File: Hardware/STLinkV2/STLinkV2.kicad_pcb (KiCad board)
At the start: 2 copper layers, 73.7 x 38.1 mm, 62 parts, among them J1 USB_B_Micro, J2 SWD, J3 ISP, J4 RS232, J5 JTAG, U1 STM32F103CBT6, U2 SRV05-4, U3 HT7833, U4 SRV05-4, U5 SRV05-4, U6 74AVCH2T45DC,125, U7 74AVCH2T45DC,125, Y1 8MHz

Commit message: Final review of 'STLinkV2' and fabrication output.
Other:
- rule pad_to_mask_clearance: 0.1 -> 0
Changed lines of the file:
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@@
       (dielectric_constraints no)
     )
-    (pad_to_mask_clearance 0.1)
-    (solder_mask_min_width 0.2)
+    (pad_to_mask_clearance 0)
     (grid_origin 63.5 50.8)
     (pcbplotparams

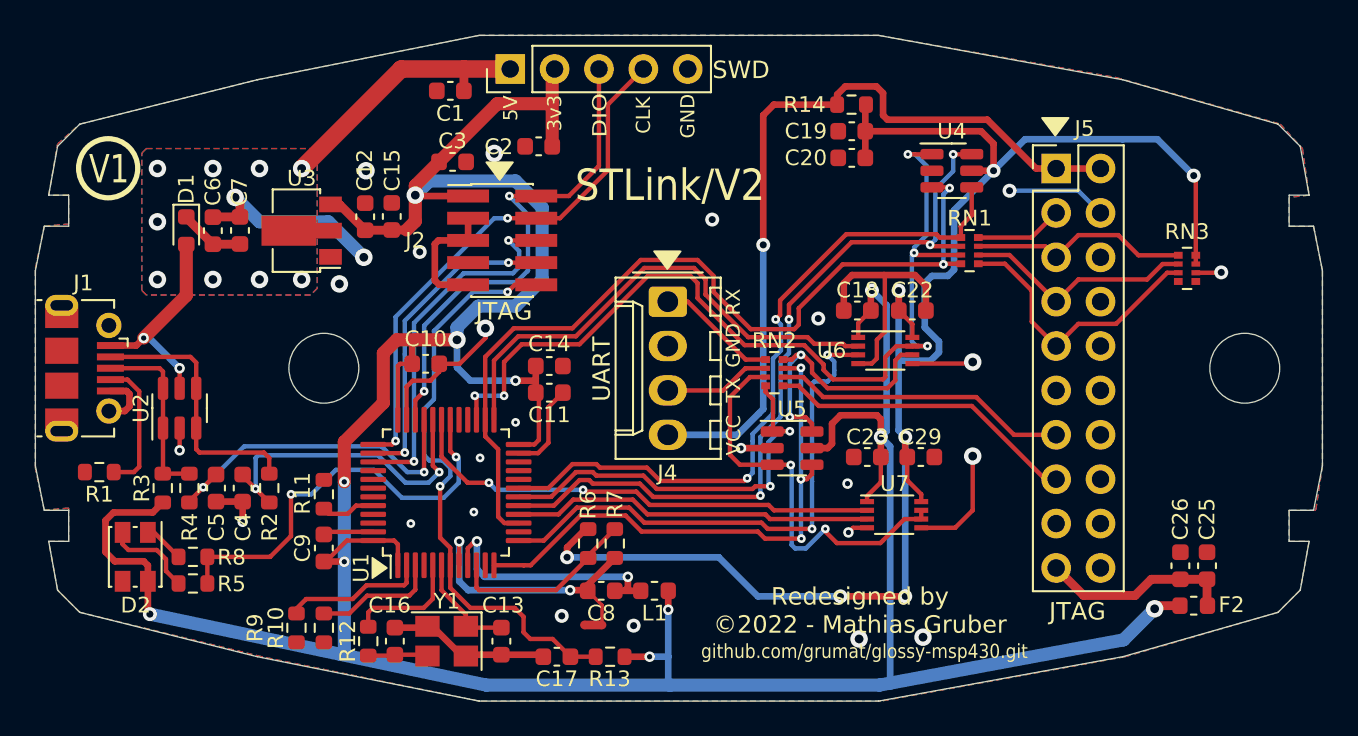
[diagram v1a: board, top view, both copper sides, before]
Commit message: Minor fixes on the STLinkV2 board (no new version is required)
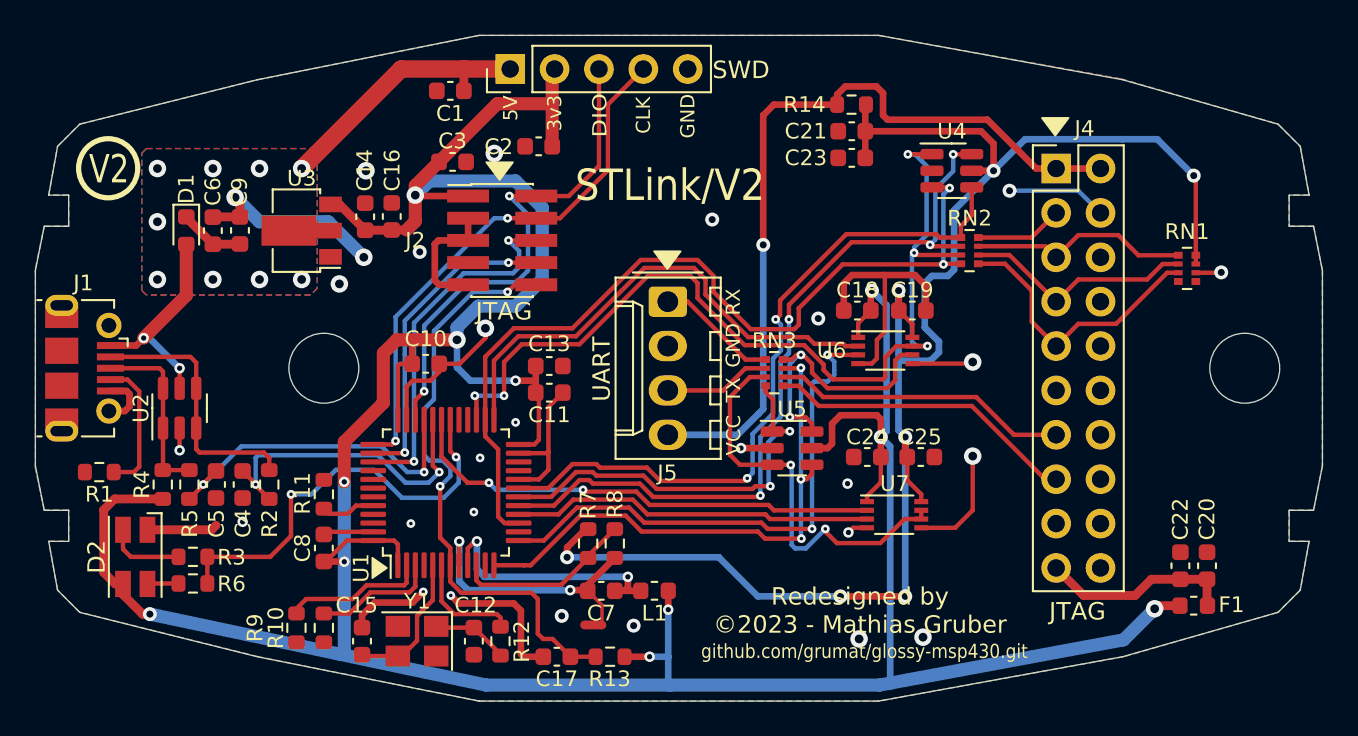
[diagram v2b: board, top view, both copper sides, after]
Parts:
- C12: renamed from C13; value 20pF -> 4.7pF
- C15: renamed from C16; value 20pF -> 4.7pF
- D2: footprint LED_SMD:LED_Kingbright_AAA3528ESGCT -> LED_SMD:LED_RGB_Wuerth-PLCC4_3.2x2.8mm_150141M173100
- R12: value 2k -> 470
- moved R12 7.57 mm to (90.1, 85.5)
- moved C15 1.88 mm to (82.2, 85.5)
- moved Y1 1.69 mm to (85.3, 85.5)
- moved C12 1.57 mm to (88.6, 85.5)
- moved R3 1.52 mm to (72.5, 80.6)
- moved R6 1.52 mm to (72.5, 82.2)
- moved C4 0.20 mm to (75.4, 76.5)
- moved C5 0.20 mm to (73.8, 76.5)
- moved R2 0.20 mm to (76.9, 76.5)
- moved R4 0.20 mm to (70.8, 76.5)
- moved R5 0.20 mm to (72.3, 76.5)
- renumbered C14 to C13, C12 to C14, C15 to C16, C22 to C19, C25 to C20, C19 to C21, C26 to C22, C20 to C23, C23 to C24, C29 to C25, C8 to C7, C9 to C8, C7 to C9, F2 to F1, J5 to J4, J4 to J5, R5 to R3, R3 to R4, R4 to R5, R8 to R6, R6 to R7, R7 to R8, RN3 to RN1, RN1 to RN2, RN2 to RN3
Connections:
- C12 pad 1: /OSC_OUT -> Net-(C12-Pad1)
- C15 pad 1: Net-(C16-Pad1) -> /OSC_IN
- R12 pad 1: Net-(C16-Pad1) -> Net-(C12-Pad1)
- R12 pad 2: /OSC_IN -> /OSC_OUT
- U1 pad 20: unconnected-(U1-Pad20) -> GND
- Y1 pad 1: /OSC_OUT -> Net-(C12-Pad1)
- Y1 pad 3: Net-(C16-Pad1) -> /OSC_IN
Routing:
- net GND: track 86.2 -> 94.5 mm, vias 26 -> 28
- net Net-(C12-Pad1): track 0.00 -> 4.41 mm
- net Net-(C16-Pad1): track 3.44 -> 0.00 mm
- net /OSC_IN: track 6.76 -> 8.24 mm
- net Net-(D2-Pad4): track 5.20 -> 4.47 mm
- net Net-(D2-Pad1): track 2.33 -> 1.79 mm
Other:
- board text added: "Redesigned by ©2023 - Mathias Gruber"
- board text added: "V2"
- board text removed: "Redesigned by ©2022 - Mathias Gruber"
- board text removed: "V1"

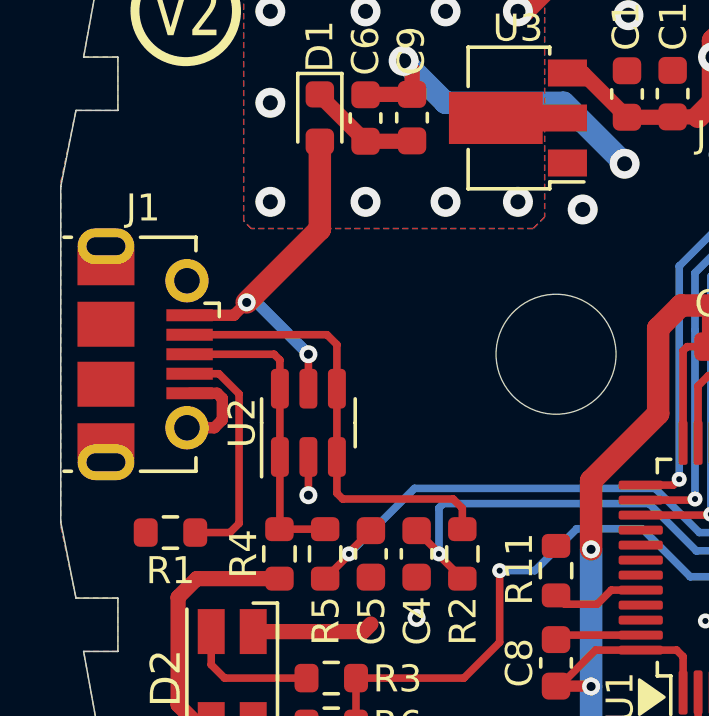
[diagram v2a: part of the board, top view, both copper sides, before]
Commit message: Fixes on USB ESD protection
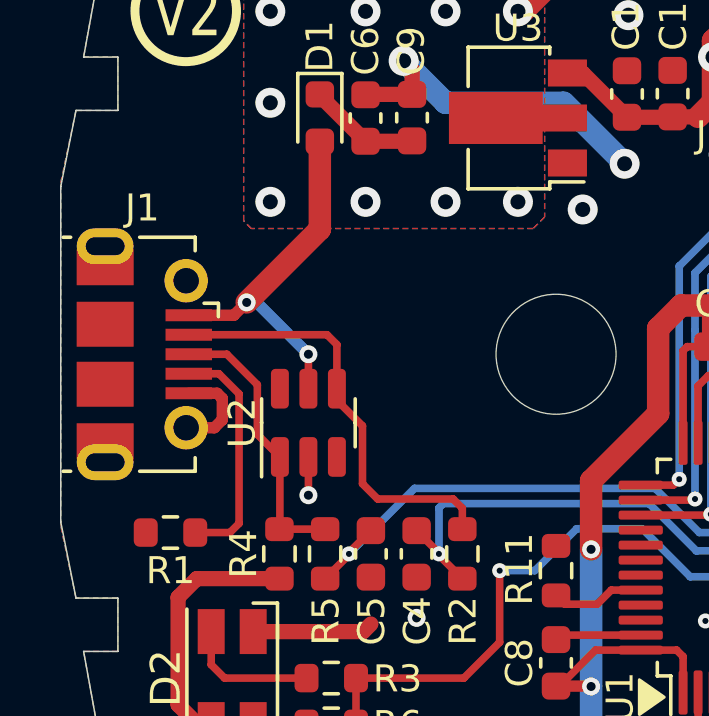
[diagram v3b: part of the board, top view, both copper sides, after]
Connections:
- U2 pad 3: /E_USB- -> unconnected-(U2-Pad3)
- U2 pad 6: /E_USB+ -> unconnected-(U2-Pad6)
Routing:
- net /E_USB+: track 10.3 -> 9.36 mm
- net /E_USB-: track 15.1 -> 14.4 mm
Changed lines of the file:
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@@
   (net 66 "unconnected-(RN1-Pad5)")
   (net 67 "Net-(R9-Pad2)")
+  (net 68 "unconnected-(U2-Pad3)")
+  (net 69 "unconnected-(U2-Pad6)")
   (footprint "Capacitor_SMD:C_0603_1608Metric" (layer "F.Cu")
     (at 75.2094 61.963 90)
@@
   )
   (footprint "lib:USB_Micro-B_Molex-105017-0001-handsolder" locked (layer "F.Cu")
-    (at 66.2447 69.85 -90)
+    (at 66.2178 69.85 -90)
     (descr "http://www.molex.com/pdm_docs/sd/1050170001_sd.pdf")
     (tags "Micro-USB SMD Typ-B")
@@
       (net 1 "GND") (pinfunction "VN") (pintype "passive"))
     (pad "3" smd roundrect (at -1.1375 0.95 90) (size 1.325 0.6) (layers "F.Cu" "F.Paste" "F.Mask") (roundrect_rratio 0.25)
-      (net 34 "/E_USB-") (pinfunction "IO2") (pintype "passive"))
+      (net 68 "unconnected-(U2-Pad3)") (pinfunction "IO2") (pintype "passive+no_connect"))
     (pad "4" smd roundrect (at 1.1375 0.95 90) (size 1.325 0.6) (layers "F.Cu" "F.Paste" "F.Mask") (roundrect_rratio 0.25)
       (net 34 "/E_USB-") (pinfunction "IO3") (pintype "passive"))
@@
       (net 4 "VBUS") (pinfunction "VP") (pintype "passive"))
     (pad "6" smd roundrect (at 1.1375 -0.95 90) (size 1.325 0.6) (layers "F.Cu" "F.Paste" "F.Mask") (roundrect_rratio 0.25)
-      (net 35 "/E_USB+") (pinfunction "IO4") (pintype "passive"))
+      (net 69 "unconnected-(U2-Pad6)") (pinfunction "IO4") (pintype "passive+no_connect"))
     (model "${KICAD6_3DMODEL_DIR}/Package_TO_SOT_SMD.3dshapes/SOT-23-6.wrl"
       (offset (xyz 0 0 0))
@@
   (segment (start 113.8428 64.516) (end 112.0648 64.516) (width 0.381) (layer "F.Cu") (net 1))
   (segment (start 112.0648 64.516) (end 110.236 64.516) (width 0.381) (layer "F.Cu") (net 1))
-  (segment (start 67.7947 71.15) (end 68.7116 71.15) (width 0.381) (layer "F.Cu") (net 1))
   (segment (start 86.614 70.0532) (end 86.614 69.596) (width 0.254) (layer "F.Cu") (net 1))
   (segment (start 110.236 64.516) (end 109.7658 64.9862) (width 0.381) (layer "F.Cu") (net 1))
@@
   (segment (start 114.4654 66.548) (end 114.4654 65.1386) (width 0.381) (layer "F.Cu") (net 1))
   (segment (start 75.2094 60.3504) (end 74.93 60.071) (width 0.508) (layer "F.Cu") (net 1))
+  (segment (start 68.7116 71.15) (end 67.7678 71.15) (width 0.381) (layer "F.Cu") (net 1))
   (segment (start 117.0552 69.584) (end 117.1448 69.4944) (width 0.254) (layer "F.Cu") (net 1))
   (segment (start 112.1156 64.5668) (end 112.0648 64.516) (width 0.254) (layer "F.Cu") (net 1))
@@
   (segment (start 81.1784 76.3524) (end 81.1784 80.9244) (width 0.75) (layer "B.Cu") (net 3))
   (segment (start 87.63 67.5132) (end 88.8492 66.294) (width 0.75) (layer "B.Cu") (net 3))
-  (segment (start 67.7947 68.55) (end 69.2704 68.55) (width 0.381) (layer "F.Cu") (net 4))
-  (segment (start 69.2704 68.55) (end 69.6976 68.1228) (width 0.381) (layer "F.Cu") (net 4))
+  (segment (start 69.2704 68.55) (end 67.7678 68.55) (width 0.381) (layer "F.Cu") (net 4))
   (segment (start 71.755 70.9985) (end 71.755 69.85) (width 0.254) (layer "F.Cu") (net 4))
   (segment (start 69.6976 68.1228) (end 72.136 65.6844) (width 0.75) (layer "F.Cu") (net 4))
+  (segment (start 69.6976 68.1228) (end 69.2704 68.55) (width 0.381) (layer "F.Cu") (net 4))
   (segment (start 72.136 65.6844) (end 72.136 62.7635) (width 0.75) (layer "F.Cu") (net 4))
   (via (at 71.755 69.85) (size 0.6) (drill 0.3) (layers "F.Cu" "B.Cu") (net 4))
@@
   (segment (start 126.4412 82.8548) (end 127.368 81.928) (width 0.508) (layer "F.Cu") (net 5))
   (segment (start 127.368 81.928) (end 129.032 81.928) (width 0.508) (layer "F.Cu") (net 5))
-  (segment (start 68.7714 70.5) (end 69.4436 71.1722) (width 0.254) (layer "F.Cu") (net 6))
-  (segment (start 69.4436 71.1722) (end 69.4436 75.4888) (width 0.254) (layer "F.Cu") (net 6))
-  (segment (start 69.4436 75.4888) (end 69.1388 75.7936) (width 0.254) (layer "F.Cu") (net 6))
-  (segment (start 67.7947 70.5) (end 68.7714 70.5) (width 0.254) (layer "F.Cu") (net 6))
-  (segment (start 69.1388 75.7936) (end 67.9826 75.7936) (width 0.254) (layer "F.Cu") (net 6))
+  (segment (start 69.4436 71.1722) (end 68.7714 70.5) (width 0.254) (layer "F.Cu") (net 6))
+  (segment (start 68.7714 70.5) (end 67.7678 70.5) (width 0.254) (layer "F.Cu") (net 6))
+  (segment (start 69.1388 75.7936) (end 69.4436 75.4888) (width 0.254) (layer "F.Cu") (net 6))
+  (segment (start 69.4436 75.4888) (end 69.4436 71.1722) (width 0.254) (layer "F.Cu") (net 6))
+  (segment (start 67.9826 75.7936) (end 69.1388 75.7936) (width 0.254) (layer "F.Cu") (net 6))
   (segment (start 93.0188 77.212) (end 91.1575 77.212) (width 0.254) (layer "F.Cu") (net 7))
   (segment (start 104.6988 76.6064) (end 104.5464 76.7588) (width 0.254) (layer "F.Cu") (net 7))
@@
   (segment (start 88.773 79.756) (end 88.773 81.3562) (width 0.381) (layer "B.Cu") (net 33))
   (segment (start 88.773 81.3562) (end 89.2048 81.788) (width 0.381) (layer "B.Cu") (net 33))
-  (segment (start 72.705 74.483) (end 72.898 74.676) (width 0.254) (layer "F.Cu") (net 34))
-  (segment (start 72.705 73.2735) (end 72.705 74.483) (width 0.254) (layer "F.Cu") (net 34))
+  (segment (start 72.705 69.53) (end 72.375 69.2) (width 0.254) (layer "F.Cu") (net 34))
   (segment (start 76.581 74.676) (end 76.8858 74.9808) (width 0.254) (layer "F.Cu") (net 34))
-  (segment (start 67.7947 69.2) (end 72.375 69.2) (width 0.254) (layer "F.Cu") (net 34))
+  (segment (start 72.375 69.2) (end 67.7678 69.2) (width 0.254) (layer "F.Cu") (net 34))
+  (segment (start 73.5584 74.168) (end 74.0664 74.676) (width 0.254) (layer "F.Cu") (net 34))
+  (segment (start 72.705 71.3842) (end 73.5584 72.2376) (width 0.254) (layer "F.Cu") (net 34))
   (segment (start 72.705 70.9985) (end 72.705 69.53) (width 0.254) (layer "F.Cu") (net 34))
-  (segment (start 72.705 73.2735) (end 72.705 70.9985) (width 0.254) (layer "F.Cu") (net 34))
-  (segment (start 72.705 69.53) (end 72.375 69.2) (width 0.254) (layer "F.Cu") (net 34))
+  (segment (start 72.705 70.9985) (end 72.705 71.3842) (width 0.254) (layer "F.Cu") (net 34))
+  (segment (start 73.5584 72.2376) (end 73.5584 74.168) (width 0.254) (layer "F.Cu") (net 34))
+  (segment (start 74.0664 74.676) (end 76.581 74.676) (width 0.254) (layer "F.Cu") (net 34))
   (segment (start 76.8858 74.9808) (end 76.8858 75.6798) (width 0.254) (layer "F.Cu") (net 34))
-  (segment (start 72.898 74.676) (end 76.581 74.676) (width 0.254) (layer "F.Cu") (net 34))
-  (segment (start 70.805 70.043) (end 70.612 69.85) (width 0.254) (layer "F.Cu") (net 35))
-  (segment (start 67.7947 69.85) (end 70.612 69.85) (width 0.254) (layer "F.Cu") (net 35))
-  (segment (start 70.805 73.2735) (end 70.805 70.9985) (width 0.254) (layer "F.Cu") (net 35))
-  (segment (start 70.805 70.9985) (end 70.805 70.043) (width 0.254) (layer "F.Cu") (net 35))
+  (segment (start 70.0532 72.5217) (end 70.0532 70.866) (width 0.254) (layer "F.Cu") (net 35))
+  (segment (start 70.805 73.2735) (end 70.0532 72.5217) (width 0.254) (layer "F.Cu") (net 35))
   (segment (start 70.7898 75.6798) (end 72.3138 75.6798) (width 0.254) (layer "F.Cu") (net 35))
   (segment (start 70.805 75.6646) (end 70.7898 75.6798) (width 0.254) (layer "F.Cu") (net 35))
+  (segment (start 70.0532 70.866) (end 69.0372 69.85) (width 0.254) (layer "F.Cu") (net 35))
+  (segment (start 69.0372 69.85) (end 67.7678 69.85) (width 0.254) (layer "F.Cu") (net 35))
   (segment (start 70.805 73.2735) (end 70.805 75.6646) (width 0.254) (layer "F.Cu") (net 35))
   (segment (start 73.1074 76.5048) (end 73.1074 76.5362) (width 0.254) (layer "F.Cu") (net 36))

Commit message: Relabeled SWD lines on STLinkV2 schematics, since they were misleading.
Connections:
- net /TMS renamed /SWD_IN
- net /TMS_SWDIO renamed /TMS_SWDO
